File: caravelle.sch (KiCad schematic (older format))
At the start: 83 parts, among them J1 Conn_01x04, J2 Conn_01x02_Female, J3 Conn_01x04, J4 Conn_01x02_Female, K1 keyboard_parts_KEYSW, K10 keyboard_parts_KEYSW, K11 keyboard_parts_KEYSW, K12 keyboard_parts_KEYSW, K13 keyboard_parts_KEYSW, K14 keyboard_parts_KEYSW, K15 keyboard_parts_KEYSW, K16 keyboard_parts_KEYSW, K17 keyboard_parts_KEYSW, K18 keyboard_parts_KEYSW, K19 keyboard_parts_KEYSW, K2 keyboard_parts_KEYSW, K20 keyboard_parts_KEYSW, K21 keyboard_parts_KEYSW, K22 keyboard_parts_KEYSW, K23 keyboard_parts_KEYSW, K24 keyboard_parts_KEYSW, K25 keyboard_parts_KEYSW, K26 keyboard_parts_KEYSW, K27 keyboard_parts_KEYSW, K28 keyboard_parts_KEYSW, K29 keyboard_parts_KEYSW, K3 keyboard_parts_KEYSW, K30 keyboard_parts_KEYSW, K31 keyboard_parts_KEYSW, K32 keyboard_parts_KEYSW, K33 keyboard_parts_KEYSW, K34 keyboard_parts_KEYSW, K35 keyboard_parts_KEYSW, K36 keyboard_parts_KEYSW, K37 keyboard_parts_KEYSW, K38 keyboard_parts_KEYSW, K39 keyboard_parts_KEYSW, K4 keyboard_parts_KEYSW, K40 keyboard_parts_KEYSW, K41 keyboard_parts_KEYSW, K42 keyboard_parts_KEYSW, K43 keyboard_parts_KEYSW, K44 keyboard_parts_KEYSW, K45 keyboard_parts_KEYSW, K46 keyboard_parts_KEYSW, K47 keyboard_parts_KEYSW, K48 keyboard_parts_KEYSW, K5 keyboard_parts_KEYSW, K6 keyboard_parts_KEYSW, K7 keyboard_parts_KEYSW, K8 keyboard_parts_KEYSW, K9 keyboard_parts_KEYSW, SW1 SW_SPDT, SW2 SW_SPDT, U1 MDBT40_LEFT, U10 STLQ015M33R, U11 logo1, U12 logo2, U13 logo1, U2 hole, U3 hole, U4 hole, U5 MDBT40_RIGHT, U6 hole, U7 hole, U8 hole, U9 STLQ015M33R, Y1 32.768kHz, Y2 32.768kHz

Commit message: Add v2.0 PCB
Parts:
- removed C2, C3, C5, C6: 12pF, Capacitor_SMD:C_0603_1608Metric_Pad1.05x0.95mm_HandSolder, symbol Device:C
- removed U5: MDBT40_RIGHT, locallib:MDBT40, symbol MDBT40:MDBT40
- removed Y1, Y2: 32.768kHz, Crystal:Crystal_SMD_3215-2Pin_3.2x1.5mm, symbol Device:Crystal
- added R1, R2: R_Small, Resistor_SMD:R_0603_1608Metric_Pad1.05x0.95mm_HandSolder, symbol Device:R_Small
- added SW3, SW4: RESET_SW, locallib:SW_SPST_ALPS-SKRP, symbol Switch:SW_Push
- added U5: BL652_RIGHT, RF_Module:Laird_BL652, symbol RF_Bluetooth:BL652
- C1, C4: value 1uF -> 0.1uF
- U1: value MDBT40_LEFT -> BL652_LEFT; footprint locallib:MDBT40 -> RF_Module:Laird_BL652; symbol MDBT40:MDBT40 -> RF_Bluetooth:BL652
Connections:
- net XL1 is gone; now on net L1: U1.10 (SIO_16)
- net XL2 is gone; now on net L7: U1.9 (SIO_18)
- net GND: now also U1.16 (GND), U1.27 (GND), U1.39 (GND), SW3.2; no longer U1.13 (GND), U1.2 (GND), U1.25 (GND), U1.42 (GND)
- net GNDA: now also SW4.2, U5.1 (GND), U5.16 (GND), U5.27 (GND), U5.39 (GND)
- net L1: no longer U1.22 (P0.05)
- net L10: now also U1.21 (SIO_04/AIN2); no longer U1.17 (P0.00)
- net L11: now also U1.28 (SIO_13); no longer U1.31 (P0.13)
- net L12: now also U1.31 (SIO_19); no longer U1.34 (P0.16)
- net L13: now also U1.33 (SIO_30/AIN6); no longer U1.28 (P0.10)
- net L14: now also U1.8 (SIO_20); no longer U1.24 (P0.07)
- net L15: now also U1.11 (SIO_14); no longer U1.19 (P0.02)
- net L16: now also U1.17 (SIO_08); no longer U1.5 (P0.22)
- net L17: now also U1.20 (SIO_05/AIN3); no longer U1.16 (P0.30)
- net L18: now also U1.23 (SIO_02/AIN0); no longer U1.30 (P0.12)
- net L19: now also U1.30 (SIO_17); no longer U1.33 (P0.15)
- net L2: now also U1.13 (SIO_11); no longer U1.21 (P0.04)
- net L20: now also U1.34 (SIO_29/AIN5); no longer U1.27 (P0.09)
- net L21: now also U1.35 (SIO_28/AIN4); no longer U1.37 (P0.17)
- net L22: now also U1.36 (SIO_27); no longer U1.38 (P0.18)
- net L23: now also U1.37 (SIO_26); no longer U1.39 (P0.19)
- net L24: now also U1.38 (SIO_25); no longer U1.40 (P0.20)
- net L3: now also U1.19 (SIO_06); no longer U1.7 (P0.24)
- net L4: now also U1.22 (SIO_03/AIN1); no longer U1.18 (P0.01)
- net L5: now also U1.29 (SIO_15); no longer U1.32 (P0.14)
- net L6: now also U1.32 (SIO_31/AIN7); no longer U1.29 (P0.11)
- net L7: no longer U1.23 (P0.06)
- net L8: now also U1.12 (SIO_12); no longer U1.20 (P0.03)
- net L9: now also U1.18 (SIO_07); no longer U1.6 (P0.23)
- net R1: now also U5.31 (SIO_19)
- net R10: now also U5.19 (SIO_06)
- net R11: now also U5.15 (SIO_09/NFC1)
- net R12: now also U5.12 (SIO_12)
- net R13: now also U5.10 (SIO_16)
- net R14: now also U5.33 (SIO_30/AIN6)
- net R15: now also U5.28 (SIO_13)
- net R16: now also U5.21 (SIO_04/AIN2)
- net R17: now also U5.18 (SIO_07)
- net R18: now also U5.14 (SIO_10/NFC2)
- net R19: now also U5.11 (SIO_14)
- net R2: now also U5.30 (SIO_17)
- net R20: now also U5.9 (SIO_18)
- net R21: now also U5.8 (SIO_20)
- net R22: now also U5.4 (SIO_22)
- net R23: now also U5.3 (SIO_23)
- net R24: now also U5.2 (SIO_24)
- net R3: now also U5.23 (SIO_02/AIN0)
- net R4: now also U5.20 (SIO_05/AIN3)
- net R5: now also U5.17 (SIO_08)
- net R6: now also U5.13 (SIO_11)
- net R7: now also U5.32 (SIO_31/AIN7)
- net R8: now also U5.29 (SIO_15)
- net R9: now also U5.22 (SIO_03/AIN1)
- net SWDCLK: now also U1.6 (SWDCLK); no longer U1.36 (SWDCLK)
- net SWDCLK_R: now also U5.6 (SWDCLK)
- net SWDIO: now also U1.5 (SWDIO); no longer U1.35 (SWDIO/RESET)
- net SWDIO_R: now also U5.5 (SWDIO)
- net VAA: now also U5.26 (VDD)
- net VCC: now also U1.26 (VDD); no longer U1.14 (VDD), U1.3 (AVDD)
- net at D1.1 (K), SW1.3 (C): now also R1.1
- net at D1.2 (A), J2.1 (Pin_1): now also R1.2
- net at D3.1 (K), SW2.2 (B): now also R2.1
- net at D3.2 (A), J4.1 (Pin_1): now also R2.2
- new net: SW3.1, U1.7 (SIO_21)
- new net: SW4.1, U5.7 (SIO_21)
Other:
- note added: "BL652 MODULE"
- note removed: "MDBT40 MODULE"
- moved on the sheet: C1, D1, D3, SW1, SW2

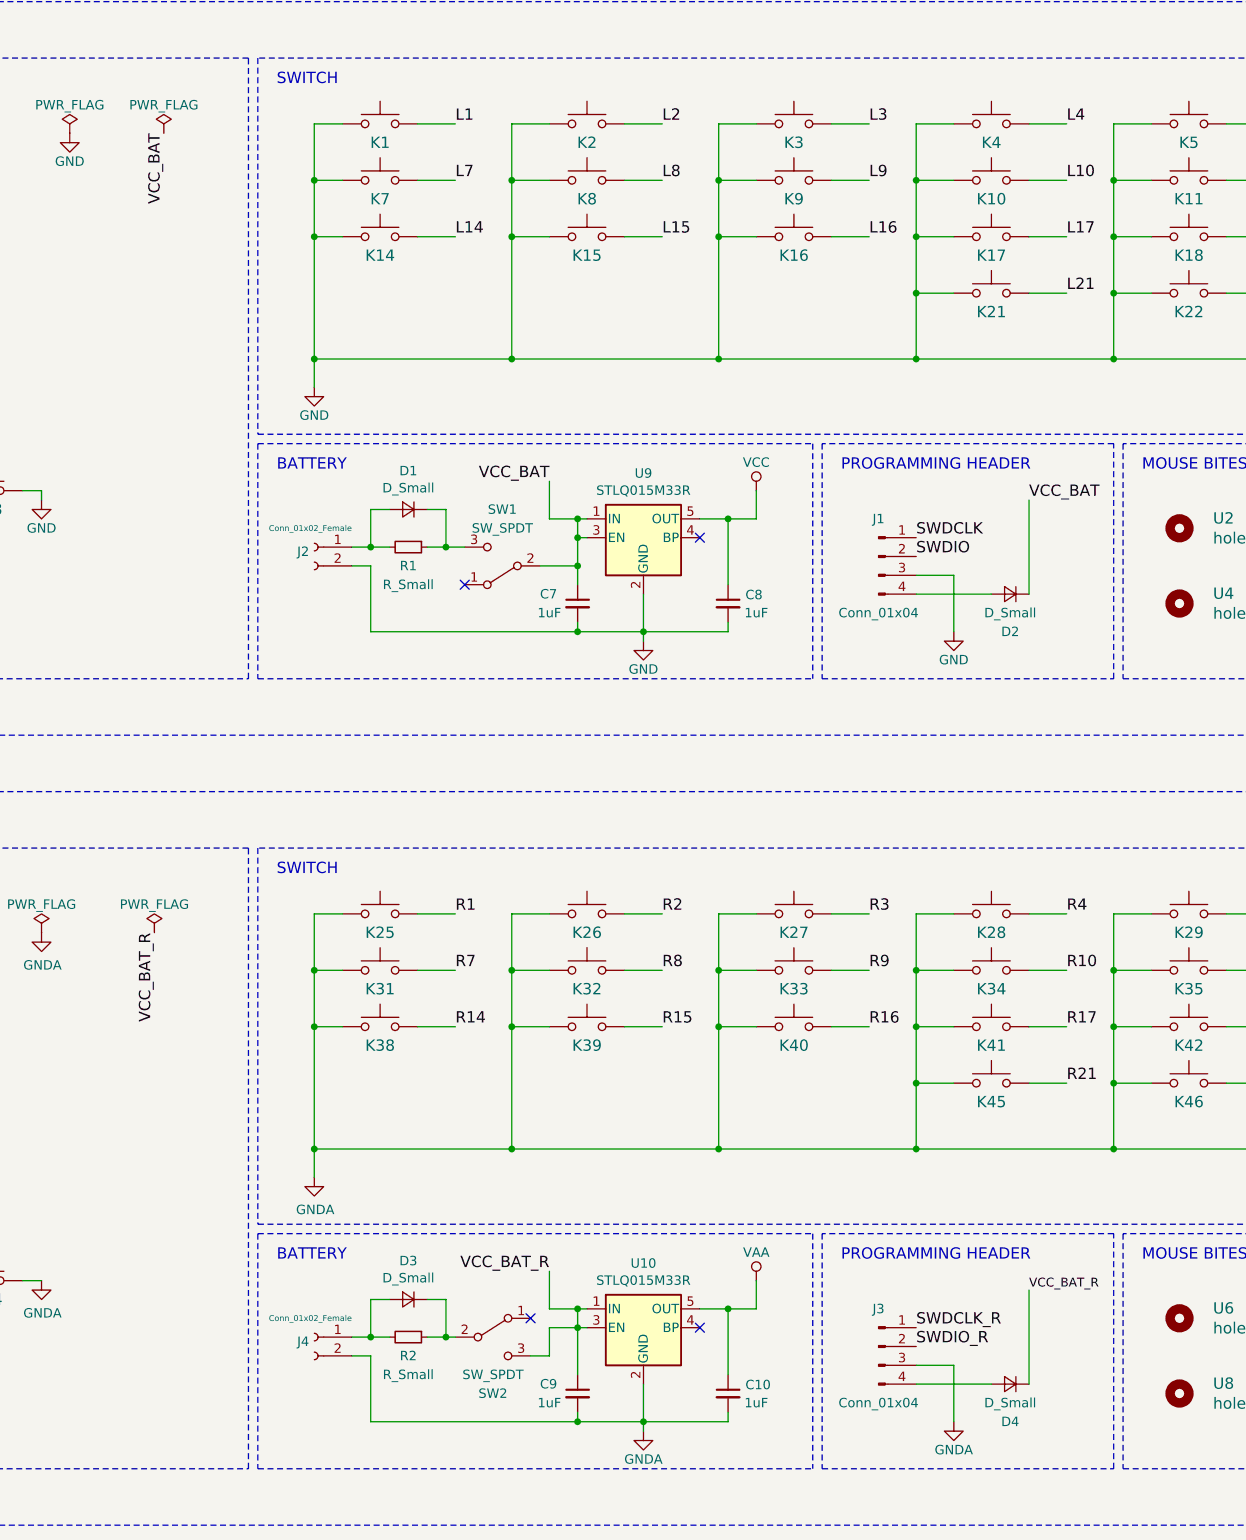
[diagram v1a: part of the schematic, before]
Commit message: Delete regulator
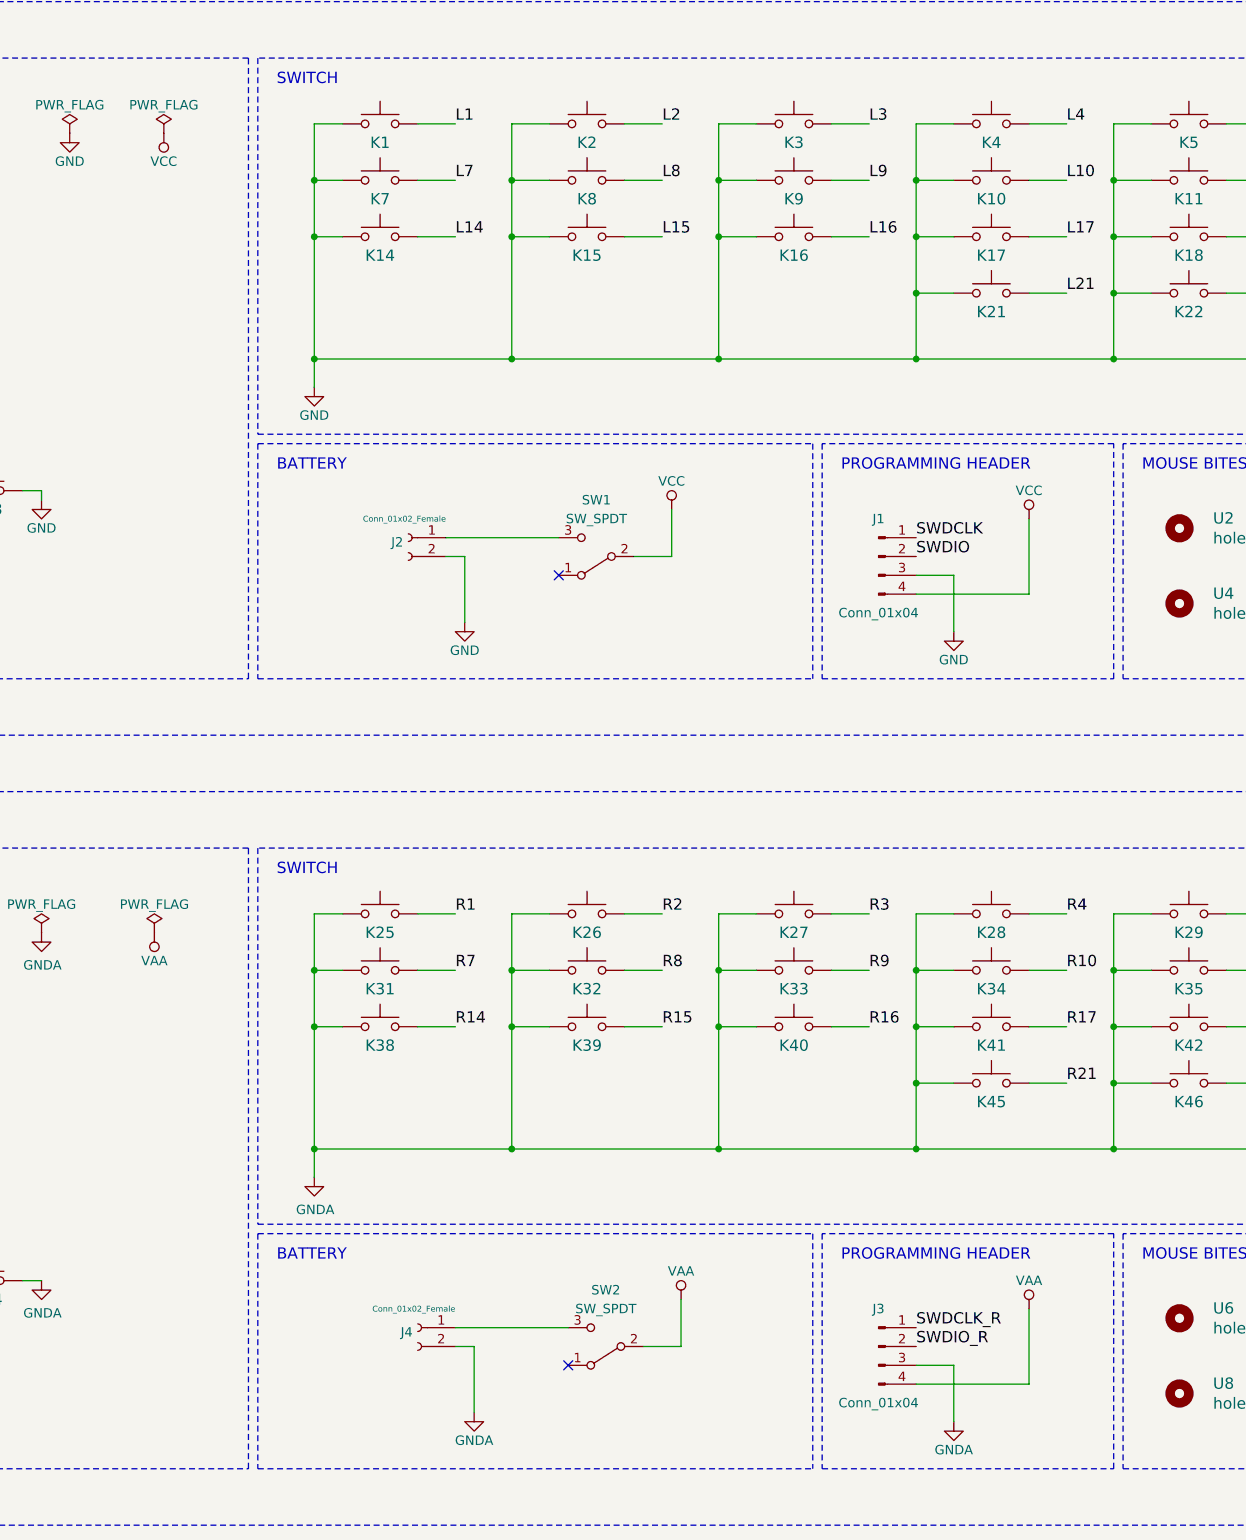
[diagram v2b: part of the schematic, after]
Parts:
- removed C10, C7, C8, C9: 1uF, Capacitor_SMD:C_0603_1608Metric_Pad1.05x0.95mm_HandSolder, symbol Device:C_Small
- removed D1, D2, D3, D4: D_Small, Diode_SMD:D_SOD-123, symbol Device:D_Small
- removed R1, R2: R_Small, Resistor_SMD:R_0603_1608Metric_Pad1.05x0.95mm_HandSolder, symbol Device:R_Small
- removed U10, U9: STLQ015M33R, TO_SOT_Packages_SMD:SOT-23-5, symbol Regulator_Linear:MIC5205-3.3YM5
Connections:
- net VCC_BAT is gone; now on net VCC: SW1.2 (B)
- net VCC_BAT_R is gone; now on an unnamed net: SW2.3 (C)
- net VAA: now also J3.4 (Pin_4), SW2.2 (B)
- net VCC: now also J1.4 (Pin_4)
- net at SW1.3 (C): now also J2.1 (Pin_1)
- no-connect marks 19 -> 17
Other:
- moved on the sheet: J2, J4, SW1
